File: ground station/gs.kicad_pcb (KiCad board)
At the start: 2 copper layers, 15 parts, among them J1 USB_C_Receptacle_USB2.0_14P, J2 OLED, U1 ATSAMD21G18A-A

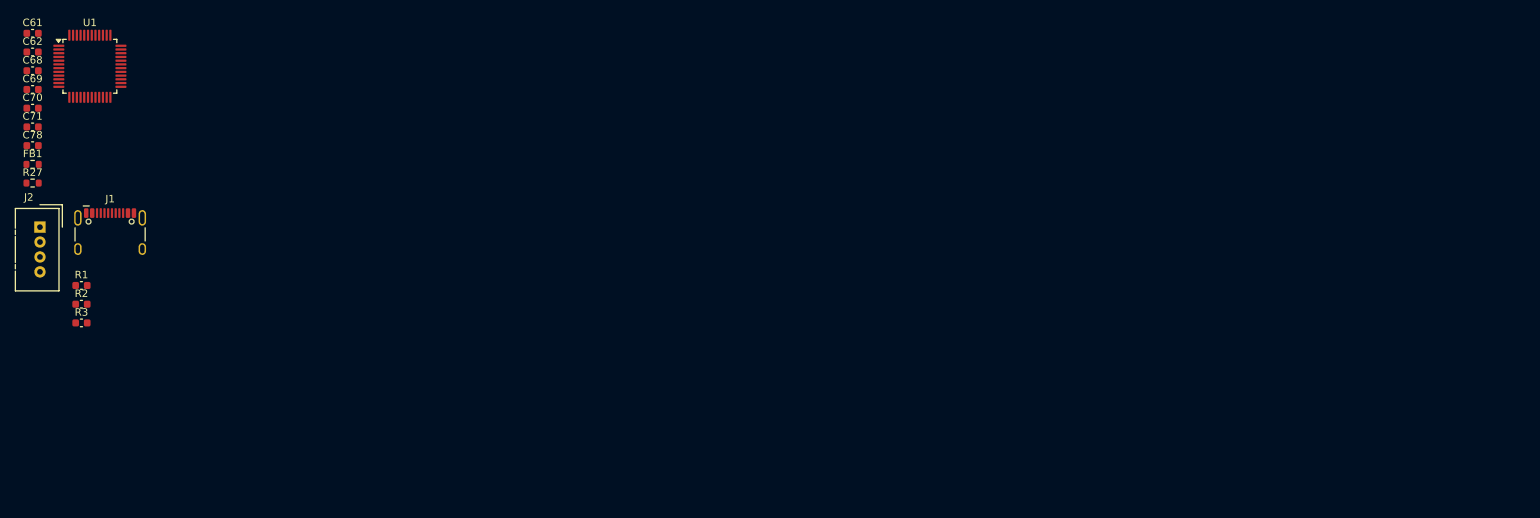
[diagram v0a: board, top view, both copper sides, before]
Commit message: schematic fixes (3.3V and stuff) + started pcb
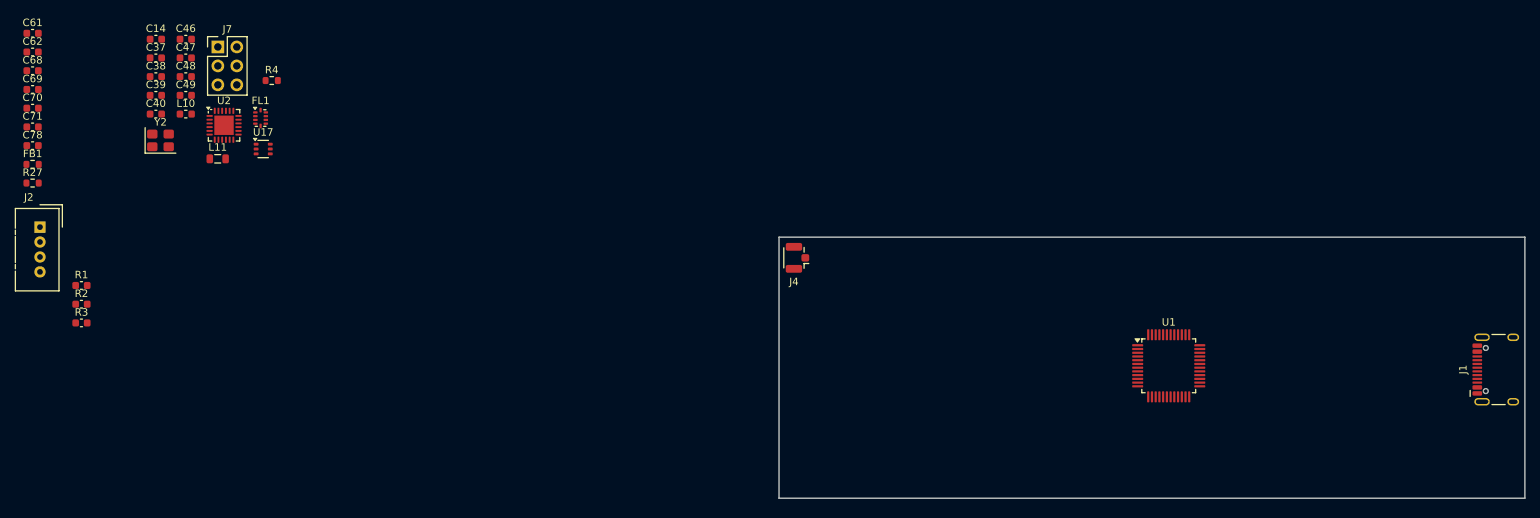
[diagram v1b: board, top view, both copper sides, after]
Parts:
- added C14: 8pF, Capacitor_SMD:C_0603_1608Metric, F.Cu at (41.7, 23.2)
- added C37: 100nF, Capacitor_SMD:C_0603_1608Metric, F.Cu at (41.7, 25.7)
- added C38: 100nF, Capacitor_SMD:C_0603_1608Metric, F.Cu at (41.7, 28.2)
- added C39: 8pF, Capacitor_SMD:C_0603_1608Metric, F.Cu at (41.7, 30.7)
- added C40: 470nF, Capacitor_SMD:C_0603_1608Metric, F.Cu at (41.7, 33.2)
- added C46: 1nF, Capacitor_SMD:C_0603_1608Metric, F.Cu at (45.7, 23.2)
- added C47: 47nF, Capacitor_SMD:C_0603_1608Metric, F.Cu at (45.7, 25.7)
- added C48: 47pF, Capacitor_SMD:C_0603_1608Metric, F.Cu at (45.7, 28.2)
- added C49: 100pF, Capacitor_SMD:C_0603_1608Metric, F.Cu at (45.7, 30.7)
- added FL1: 0900FM15K0039, RF_Converter:Balun_Johanson_0900FM15K0039, F.Cu at (55.7, 33.8)
- added J4: H9161TR-ND, Connector_Coaxial:U.FL_Hirose_U.FL-R-SMT-1_Vertical, F.Cu at (127.7, 52.5)
- added J7: Conn_02x03_Counter_Clockwise, Connector_PinHeader_2.54mm:PinHeader_2x03_P2.54mm_Vertical, F.Cu at (50.0, 24.2)
- added L10: 47nH, Inductor_SMD:L_0603_1608Metric, F.Cu at (45.7, 33.2)
- added L11: 15uH, Inductor_SMD:L_0805_2012Metric, F.Cu at (50.0, 39.2)
- added R4: 100, Resistor_SMD:R_0603_1608Metric, F.Cu at (57.2, 28.8)
- added U17: PE4259, Package_TO_SOT_SMD:SOT-363_SC-70-6, F.Cu at (56.1, 37.9)
- added U2: SX1262IMLTRT, Package_DFN_QFN:QFN-24-1EP_4x4mm_P0.5mm_EP2.6x2.6mm, F.Cu at (50.8, 34.8)
- added Y2: 32MHz, Crystal:Crystal_SMD_3225-4Pin_3.2x2.5mm, F.Cu at (42.3, 36.8)
- moved J1 187.8 mm to (222.6, 67.5), turned to 90 degrees
- moved U1 150.1 mm to (177.5, 67.0)
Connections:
- U1 pad 21: MOSI TMCU -> MOSI
- U1 pad 22: SCK TMCU -> SCK
- U1 pad 23: MISO TMCU -> MISO
- U1 pad 25: unconnected-(U1-PA16-Pad25) -> SX_NRST
- U1 pad 26: unconnected-(U1-PA17-Pad26) -> SX_DIO1
- U1 pad 27: unconnected-(U1-PA18-Pad27) -> RF_CS
- U1 pad 28: unconnected-(U1-PA19-Pad28) -> SX_BUSY
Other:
- board outline added: 100 x 35 mm

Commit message: more pcb stuff's
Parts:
- added C36: 1uF, Capacitor_SMD:C_0603_1608Metric, F.Cu at (207.8, 64.5)
- added U3: AMS1117-3.3, Package_TO_SOT_SMD:SOT-223-3_TabPin2, F.Cu at (213.0, 65.8)
- moved J7 173.1 mm to (220.9, 51.6)
- moved J2 152.4 mm to (175.0, 81.0), turned to 90 degrees
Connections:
- J2 pad 2: VCC -> +3.3V
- U1 pad 31: unconnected-(U1-PA22-Pad31) -> SDA
- U1 pad 32: unconnected-(U1-PA23-Pad32) -> SCL
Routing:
- net +3.3V: track 0.00 -> 40.2 mm
- net SCL: track 0.00 -> 18.8 mm
- net SDA: track 0.00 -> 18.7 mm
- net GND: track 0.00 -> 12.8 mm, vias 0 -> 8
- net Net-(J1-SHIELD): track 0.00 -> 10.4 mm, vias 0 -> 2
- net VBUS: track 0.00 -> 10.0 mm
- net D-: track 0.00 -> 2.59 mm
- net D+: track 0.00 -> 2.59 mm
- added copper zone on B.Cu, net GND
- added copper zone on F.Cu, net GND

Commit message: lots of RF stuff done!
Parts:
- added AE1: Antenna, Connector_PinSocket_2.54mm:PinSocket_1x01_P2.54mm_Vertical, B.Cu at (146.3, 46.9)
- added C24: 8pF, Capacitor_SMD:C_0603_1608Metric, F.Cu at (161.6, 40.9)
- added C25: 8pF, Capacitor_SMD:C_0603_1608Metric, F.Cu at (169.3, 47.6)
- added C57: 47nF, Capacitor_SMD:C_0603_1608Metric, F.Cu at (162.0, 46.9)
- added C62: 47pF, Capacitor_SMD:C_0603_1608Metric, F.Cu at (160.5, 47.3)
- added C63: 100pF, Capacitor_SMD:C_0603_1608Metric, F.Cu at (149.5, 46.1)
- added C64: 1nF, Capacitor_SMD:C_0603_1608Metric, F.Cu at (152.6, 43.8)
- added C65: 100nF, Capacitor_SMD:C_0603_1608Metric, F.Cu at (163.5, 47.2)
- added C66: 100nF, Capacitor_SMD:C_0603_1608Metric, F.Cu at (169.3, 41.1)
- added C67: 470nF, Capacitor_SMD:C_0603_1608Metric, F.Cu at (169.4, 44.6)
- added FL1: 0900FM15K0039, RF_Converter:Balun_Johanson_0900FM15K0039, F.Cu at (155.5, 46.5)
- added L10: 47nH, Inductor_SMD:L_0603_1608Metric, F.Cu at (158.3, 47.2)
- added L11: 15uH, Inductor_SMD:L_0805_2012Metric, F.Cu at (171.1, 44.4)
- added R23: 100, Resistor_SMD:R_0603_1608Metric, F.Cu at (155.6, 43.8)
- added U3: PE4259, Package_TO_SOT_SMD:SOT-363_SC-70-6, F.Cu at (152.6, 46.2)
- added U8: SX1262IMLTRT, Package_DFN_QFN:QFN-24-1EP_4x4mm_P0.5mm_EP2.6x2.6mm, F.Cu at (165.9, 43.1)
- added Y2: 32MHz, Crystal:Crystal_SMD_3225-4Pin_3.2x2.5mm, F.Cu at (166.5, 47.5)
- moved R1 187.5 mm to (219.2, 61.4)
- moved R3 185.9 mm to (217.6, 56.9)
- moved R2 185.3 mm to (216.7, 70.8), turned to -90 degrees
- moved C39 129.5 mm to (168.3, 57.7), turned to 90 degrees
- moved C40 128.5 mm to (168.4, 54.7), turned to 90 degrees
- moved C37 124.6 mm to (162.3, 57.1), turned to 90 degrees
- moved Y2 124.6 mm to (165.2, 57.3), turned to 180 degrees
- moved L11 121.0 mm to (170.0, 54.4), turned to -90 degrees
- moved C47 119.2 mm to (160.8, 57.0), turned to -90 degrees
- moved C48 117.1 mm to (159.2, 57.0), turned to -90 degrees
- moved U2 115.6 mm to (165.0, 52.9), turned to 90 degrees
- moved L10 113.8 mm to (157.0, 57.0), turned to 180 degrees
- moved C61 112.9 mm to (131.8, 59.7)
- moved C62 112.9 mm to (131.8, 62.2)
- moved C68 112.9 mm to (131.8, 64.7)
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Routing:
- net Earth: track 0.00 -> 30.5 mm, vias 0 -> 45
- net /SX_XTA: track 0.00 -> 14.4 mm, vias 0 -> 2
- net /SX_DIO2: track 0.00 -> 13.4 mm, vias 0 -> 2
- net GND: track 12.8 -> 25.0 mm, vias 8 -> 11
- net SX_RFO: track 0.00 -> 9.50 mm
- net /SX_RFO: track 0.00 -> 9.42 mm
- net SX_RFI_P: track 0.00 -> 9.29 mm
- net SX_RFI_N: track 0.00 -> 9.29 mm
- net /SX_RFI_P: track 0.00 -> 8.91 mm
- net /SX_RFI_N: track 0.00 -> 8.91 mm
- net +3V3: track 0.00 -> 8.17 mm, vias 0 -> 3
- net /SX_NRST: track 0.00 -> 7.18 mm
- net Net-(J1-CC2): track 0.00 -> 6.97 mm, vias 0 -> 2
- net SX_VR_PA: track 0.00 -> 6.44 mm
- net /SX_VR_PA: track 0.00 -> 6.28 mm
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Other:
- board text added: "-"

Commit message: 60% of the routing is done
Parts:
- removed AE1: Antenna, Connector_PinSocket_2.54mm:PinSocket_1x01_P2.54mm_Vertical
- removed C24, C25: 8pF, Capacitor_SMD:C_0603_1608Metric
- removed C57: 47nF, Capacitor_SMD:C_0603_1608Metric
- removed the C62 at (160.5, 47.3)
- removed C63: 100pF, Capacitor_SMD:C_0603_1608Metric
- removed C64: 1nF, Capacitor_SMD:C_0603_1608Metric
- removed C65, C66: 100nF, Capacitor_SMD:C_0603_1608Metric
- removed C67: 470nF, Capacitor_SMD:C_0603_1608Metric
- removed the FL1 at (155.5, 46.5)
- removed the L10 at (158.3, 47.2)
- removed the L11 at (171.1, 44.4)
- removed R23: 100, Resistor_SMD:R_0603_1608Metric
- removed the U3 at (152.6, 46.2)
- removed U8: SX1262IMLTRT, Package_DFN_QFN:QFN-24-1EP_4x4mm_P0.5mm_EP2.6x2.6mm
- removed the Y2 at (166.5, 47.5)
- added BZ2: Buzzer, Buzzer_Beeper:MagneticBuzzer_PUI_AT-0927-TT-6-R, F.Cu at (156.0, 54.7)
- added Q1: BSS138, Package_TO_SOT_SMD:SOT-23, F.Cu at (163.8, 58.0)
- added R5: 2k2, Resistor_SMD:R_0603_1608Metric, F.Cu at (166.5, 58.0)
- added REF**: TestPoint_Keystone_5019_Miniature, TestPoint:TestPoint_Keystone_5019_Miniature, B.Cu at (166.0, 52.5)
- added REF**: TestPoint_Keystone_5019_Miniature, TestPoint:TestPoint_Keystone_5019_Miniature, B.Cu at (172.0, 52.5)
- added REF**: TestPoint_Keystone_5019_Miniature, TestPoint:TestPoint_Keystone_5019_Miniature, B.Cu at (178.0, 52.5)
- added REF**: TestPoint_Keystone_5019_Miniature, TestPoint:TestPoint_Keystone_5019_Miniature, B.Cu at (169.0, 52.5)
- added REF**: TestPoint_Keystone_5019_Miniature, TestPoint:TestPoint_Keystone_5019_Miniature, B.Cu at (175.0, 52.5)
- moved R27 55.8 mm to (185.8, 65.8)
- moved J4 29.8 mm to (136.2, 81.1)
- moved C47 26.0 mm to (152.3, 81.6)
- moved C48 26.0 mm to (150.7, 81.6)
- moved L11 26.0 mm to (161.5, 79.1)
- moved U17 26.0 mm to (142.9, 80.9)
- moved C37 26.0 mm to (153.8, 81.7)
- moved C46 26.0 mm to (142.8, 78.4), turned to 180 degrees
- moved L10 26.0 mm to (148.5, 81.6)
- moved U2 26.0 mm to (156.5, 77.5)
- moved C39 26.0 mm to (159.8, 82.3)
- moved FL1 26.0 mm to (145.8, 81.0)
- moved Y2 26.0 mm to (156.7, 81.9)
- moved C40 26.0 mm to (159.9, 79.3)
- moved C38 23.1 mm to (159.9, 75.9), turned to 90 degrees
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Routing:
- net +3.3V: track 40.2 -> 135.5 mm, vias 0 -> 3
- net SX_BUSY: track 0.00 -> 35.7 mm, vias 0 -> 2
- net SX_NRST: track 0.00 -> 32.6 mm
- net SX_DIO1: track 0.00 -> 32.6 mm
- net Earth: track 30.5 -> 0.00 mm, vias 45 -> 0
- net SCK: track 0.00 -> 30.4 mm, vias 0 -> 2
- net MOSI: track 0.00 -> 27.4 mm, vias 0 -> 2
- net MISO: track 0.00 -> 26.6 mm
- net GND: track 25.0 -> 47.7 mm, vias 11 -> 29
- net BUZZER: track 0.00 -> 16.5 mm, vias 0 -> 2
- net /SX_XTA: track 14.4 -> 0.00 mm, vias 2 -> 0
- net SX_DIO2: track 0.00 -> 13.8 mm, vias 0 -> 2
- net /SX_DIO2: track 13.4 -> 0.00 mm, vias 2 -> 0
- net SX_XTA: track 3.86 -> 13.3 mm, vias 0 -> 2
- net /SX_RFO: track 9.42 -> 0.00 mm
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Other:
- board size 100 x 35 mm -> 76 x 35 mm
- board text added: "3.3V"
- board text added: "D+"
- board text added: "D-"
- board text added: "MISO"
- board text added: "MOSI"
- board text removed: "-"

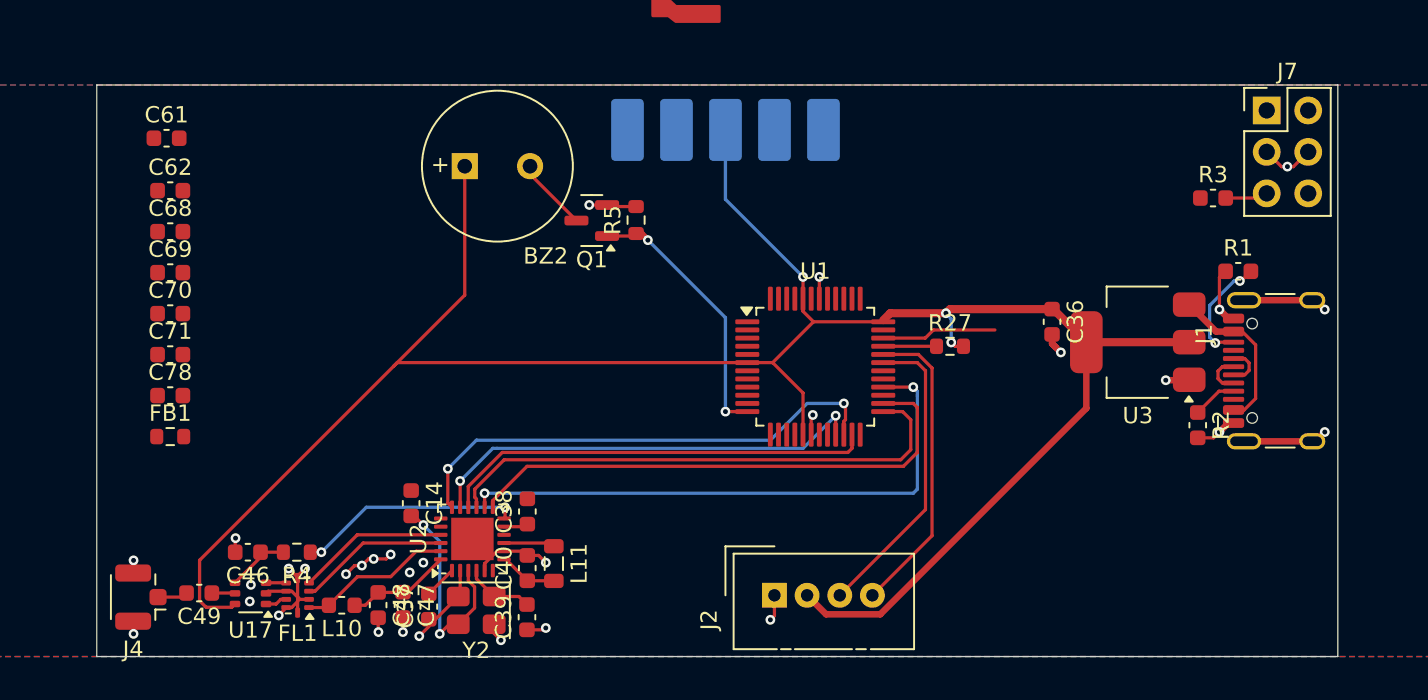
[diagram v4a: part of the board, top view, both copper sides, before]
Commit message: I think the PCB is done for the ground station
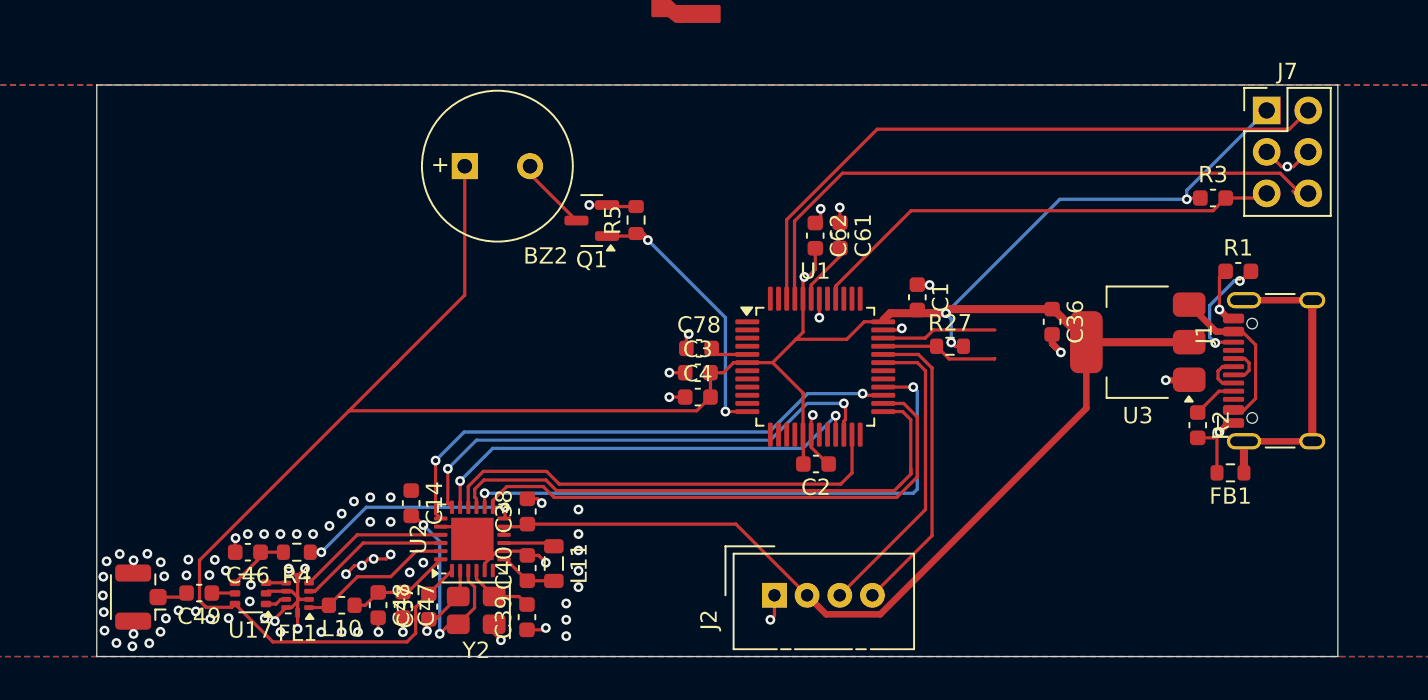
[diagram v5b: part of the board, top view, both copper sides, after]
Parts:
- removed C68, C69, C70, C71: 100nF, Capacitor_SMD:C_0603_1608Metric
- removed REF** (x5): TestPoint_Keystone_5019_Miniature, TestPoint:TestPoint_Keystone_5019_Miniature
- added C1: 100nF, Capacitor_SMD:C_0603_1608Metric, F.Cu at (183.8, 62.8)
- added C2: 100nF, Capacitor_SMD:C_0603_1608Metric, F.Cu at (177.5, 73.0)
- added C3: 100nF, Capacitor_SMD:C_0603_1608Metric, F.Cu at (170.3, 67.4)
- added C4: 100nF, Capacitor_SMD:C_0603_1608Metric, F.Cu at (170.3, 68.9)
- moved FB1 65.0 mm to (202.9, 73.5), turned to 180 degrees
- moved C61 41.7 mm to (179.0, 59.0), turned to -90 degrees
- moved C62 39.6 mm to (177.5, 59.0), turned to -90 degrees
- moved C78 32.5 mm to (170.4, 65.9)
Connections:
- C37 pad 2: +3V3 -> +3.3V
- C38 pad 1: +3V3 -> +3.3V
- U2 pad 1: +3V3 -> +3.3V
- U2 pad 10: +3V3 -> +3.3V
- U2 pad 11: +3V3 -> +3.3V
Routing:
- net +3.3V: track 135.5 -> 199.3 mm, vias 3 -> 4
- net SWDIO_FLASH: track 0.00 -> 39.5 mm
- net SWCLK_FLASH: track 0.00 -> 38.9 mm
- net RF_CS: track 0.00 -> 33.0 mm, vias 0 -> 2
- net nRESET: track 2.63 -> 29.5 mm
- net GND: track 47.7 -> 63.3 mm, vias 29 -> 82
- net Net-(J1-SHIELD): track 10.4 -> 19.3 mm, vias 2 -> 0
- net D+: track 5.85 -> 9.76 mm
- net Net-(U1-VDDCORE): track 0.00 -> 3.83 mm
- net +3V3: track 3.51 -> 0.00 mm
- net Net-(U1-GNDANA): track 0.00 -> 2.34 mm
- net SX_NRST: track 32.6 -> 34.3 mm
- net MISO: track 26.6 -> 28.1 mm
- net SX_DIO1: track 32.6 -> 33.7 mm
- net (no net): vias 0 -> 4
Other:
- board text removed: "3.3V"
- board text removed: "D+"
- board text removed: "D-"
- board text removed: "MISO"
- board text removed: "MOSI"

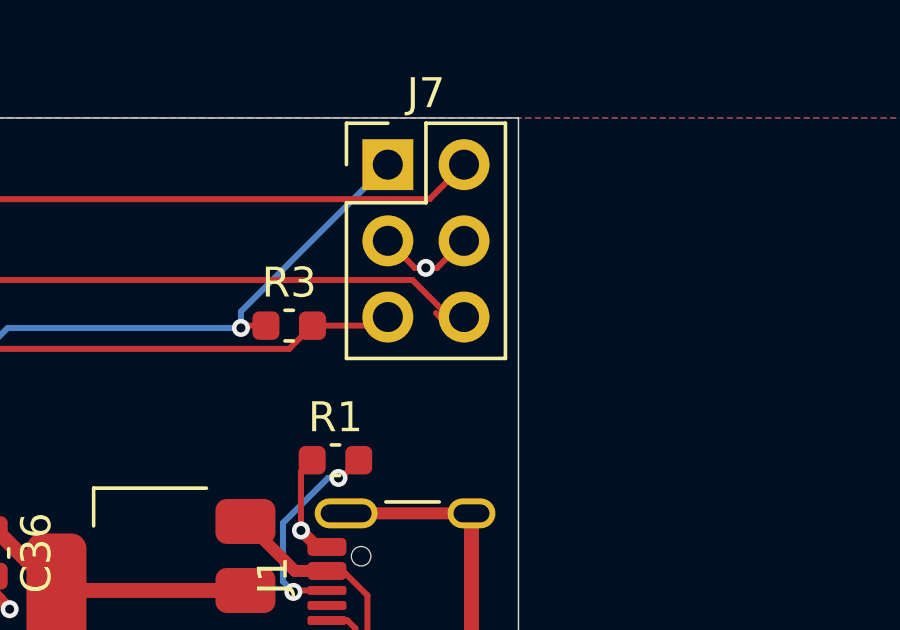
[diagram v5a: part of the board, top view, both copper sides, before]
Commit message: forgot D+ and D-... I don't want to wire it :(
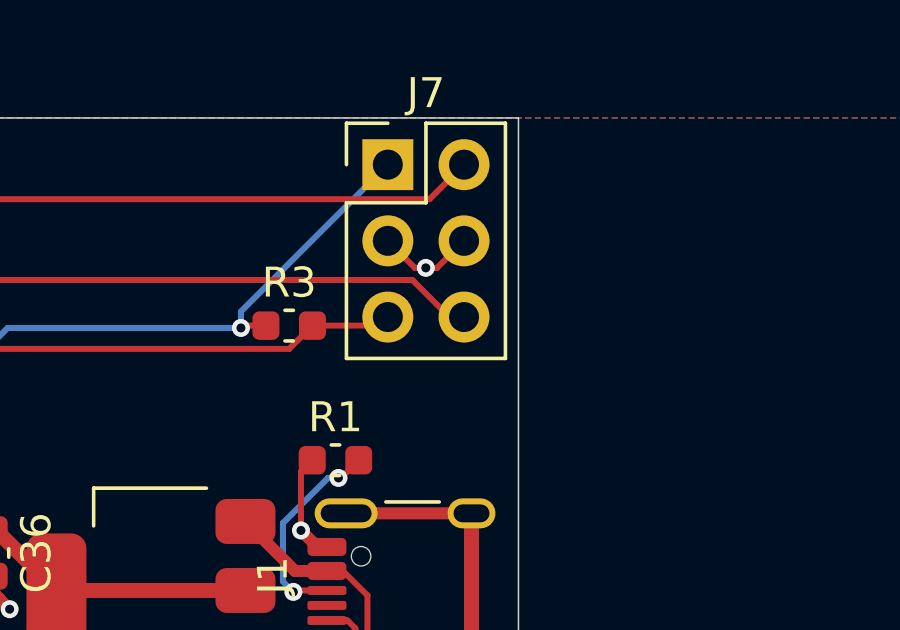
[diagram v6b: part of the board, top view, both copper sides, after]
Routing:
- net SWCLK_FLASH: track 38.9 -> 37.9 mm
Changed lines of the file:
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@@
-	)
-	(segment
-		(start 206.75 56.25)
-		(end 206.886244 56.386244)
-		(width 0.2)
-		(layer "F.Cu")
-		(net 16)
 	)
 	(segment
@@
 		(width 0.2)
 		(layer "F.Cu")
-		(net 16)
-	)
-	(segment
-		(start 206.886244 56.386244)
-		(end 207.685837 56.386244)
-		(width 0.2)
-		(layer "F.Cu")

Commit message: Data wires are routed
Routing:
- net D+: track 9.76 -> 29.5 mm, vias 0 -> 2
- net D-: track 9.63 -> 26.0 mm, vias 0 -> 2
